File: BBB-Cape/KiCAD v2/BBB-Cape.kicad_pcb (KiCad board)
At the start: 2 copper layers, 54.6 x 86.4 mm, 85 parts, among them J1 MOUNTING_HOLE, J10 Conn_01x02, J11 RJ45-TRANSFO, J12 DB9_Female, J2 MOUNTING_HOLE, J3 MOUNTING_HOLE, J4 MOUNTING_HOLE, J5 MOUNTING_HOLE, J6 MOUNTING_HOLE, J7 MOUNTING_HOLE, J8 MOUNTING_HOLE, J9 01x06_Stackable Header, P1 02x23_Stackable Header, P2 02x23_Stackable Header, SW1 W5500_RST, SW2 SYS_RST, SW3 Power, U1 LM25576MH, U2 WIZnet W5500, U3 MAX13433EETD, Y1 25MHz

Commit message: Layout start for Rev3
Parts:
- moved P1 76.2 mm to (112.6, 67.2)
- moved P2 75.7 mm to (160.8, 67.2)
- moved J9 72.0 mm to (119.1, 90.1)
- moved J1 1.96 mm to (113.9, 62.1)
- moved J4 1.54 mm to (117.0, 128.2)
- moved J3 1.30 mm to (158.9, 128.2)
- moved J2 0.92 mm to (162.2, 62.1)
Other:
- outline, holes or cut-outs redrawn
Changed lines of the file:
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@@
     (area 110.592799 47.458559 165.352801 198.739687)
     (thickness 1.6)
-    (drawings 11)
+    (drawings 12)
     (tracks 0)
     (zones 0)
@@
   )
   (module Mounting_Holes:MountingHole_3.2mm_M3_Pad (layer F.Cu)
-    (at 115.2398 63.5381)
+    (at 113.8578 62.1461)
     (descr "Mounting Hole 3.2mm, M3")
     (tags "mounting hole 3.2mm m3")
@@
   )
   (module Mounting_Holes:MountingHole_3.2mm_M3_Pad (layer F.Cu)
-    (at 161.9758 63.0301)
+    (at 162.2378 62.1461)
     (descr "Mounting Hole 3.2mm, M3")
     (tags "mounting hole 3.2mm m3")
@@
   )
   (module Mounting_Holes:MountingHole_3.2mm_M3_Pad (layer F.Cu)
-    (at 157.7848 128.8161)
+    (at 158.9078 128.1561)
     (descr "Mounting Hole 3.2mm, M3")
     (tags "mounting hole 3.2mm m3")
@@
   )
   (module Mounting_Holes:MountingHole_3.2mm_M3_Pad (layer F.Cu)
-    (at 118.4148 127.5461)
+    (at 117.0078 128.1761)
     (descr "Mounting Hole 3.2mm, M3")
     (tags "mounting hole 3.2mm m3")
@@
   )
   (module Pin_Headers:Pin_Header_Straight_1x06_Pitch2.54mm (layer F.Cu)
-    (at 137.9728 159.619499)
+    (at 119.1078 90.0961)
     (descr "Through hole straight pin header, 1x06, 2.54mm pitch, single row")
     (tags "Through hole pin header THT 1x06 2.54mm single row")
@@
   )
   (module Pin_Headers:Pin_Header_Straight_2x23_Pitch2.54mm (layer F.Cu)
-    (at 137.9728 139.05789)
+    (at 112.5678 67.2161)
     (descr "Through hole straight pin header, 2x23, 2.54mm pitch, double rows")
     (tags "Through hole pin header THT 2x23 2.54mm double row")
@@
   )
   (module Pin_Headers:Pin_Header_Straight_2x23_Pitch2.54mm (layer F.Cu)
-    (at 137.9728 139.400687)
+    (at 160.8278 67.2161)
     (descr "Through hole straight pin header, 2x23, 2.54mm pitch, double rows")
     (tags "Through hole pin header THT 2x23 2.54mm double row")
@@
     )
   )
+  (gr_line (start 122.8178 133.8961) (end 153.5678 133.8961) (layer Edge.Cuts) (width 0.15))
+  (gr_line (start 110.6678 53.8961) (end 110.6678 121.2061) (layer Edge.Cuts) (width 0.15))
+  (gr_line (start 132.1278 47.5361) (end 117.1078 47.5361) (layer Edge.Cuts) (width 0.15))
+  (gr_line (start 148.3878 47.5361) (end 159.0078 47.5361) (layer Edge.Cuts) (width 0.15))
+  (gr_line (start 165.2778 121.2061) (end 165.2778 53.8861) (layer Edge.Cuts) (width 0.15))
   (gr_line (start 148.3878 67.2161) (end 148.3878 47.5361) (layer Edge.Cuts) (width 0.15))
   (gr_line (start 132.1278 67.2161) (end 148.3838 67.2161) (layer Edge.Cuts) (width 0.15))
@@
   (gr_arc (start 123.3678 121.20626) (end 110.6678 121.20626) (angle -87.47303961) (layer Edge.Cuts) (width 0.15))
   (gr_arc (start 152.56764 121.22404) (end 165.2778 121.2215) (angle 85.5529637) (layer Edge.Cuts) (width 0.15))
-  (gr_line (start 165.2778 133.89356) (end 165.2778 47.53356) (layer Edge.Cuts) (width 0.15))
-  (gr_line (start 110.6678 133.89356) (end 165.2778 133.89356) (layer Edge.Cuts) (width 0.15))
-  (gr_line (start 110.6678 47.53356) (end 165.2778 47.53356) (layer Edge.Cuts) (width 0.15))
-  (gr_line (start 110.6678 133.89356) (end 110.6678 47.53356) (layer Edge.Cuts) (width 0.15))
 )

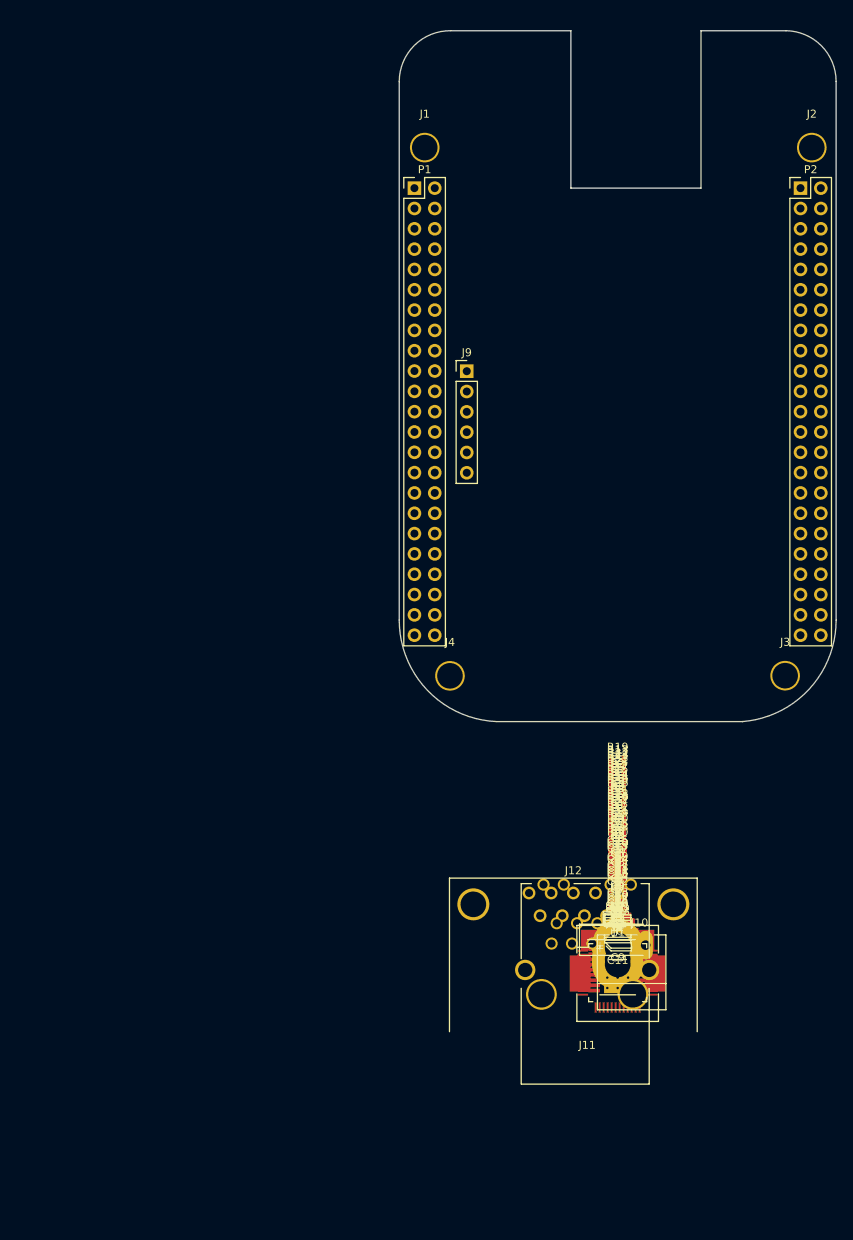
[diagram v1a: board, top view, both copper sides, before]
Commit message: Layout Update
Changed RJ45 connector to a surface mount component. Need to properly reposition P8 and P9.
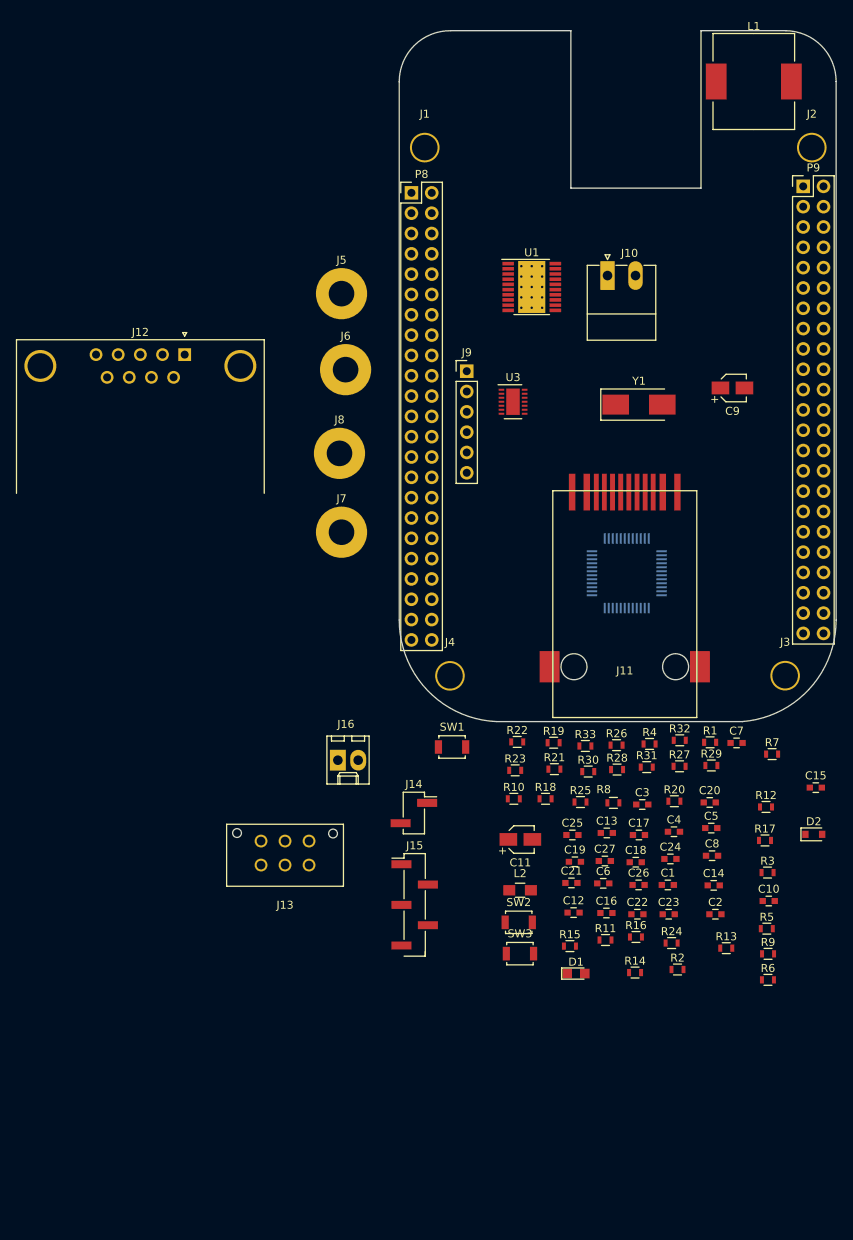
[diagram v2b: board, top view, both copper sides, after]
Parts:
- removed P1, P2: 02x23_Stackable Header, Pin_Headers:Pin_Header_Straight_2x23_Pitch2.54mm
- added J13: SPI1, Connectors_Molex:Molex_Microfit3_Header_02x03_Straight_43045-0628, F.Cu at (99.4, 151.8)
- added J14: I2C2, Pin_Headers:Pin_Header_Straight_1x02_Pitch2.54mm_SMD_Pin1Right, F.Cu at (112.5, 145.3)
- added J15: UART5, Pin_Headers:Pin_Header_Straight_1x05_Pitch2.54mm_SMD_Pin1Left, F.Cu at (112.6, 156.8)
- added J16: 5V PWR, Connectors_Molex:Molex_KK-6410-02_02x2.54mm_Straight, F.Cu at (103.0, 138.7)
- added P8: 02x23_Stackable Header, Pin_Headers:Pin_Header_Straight_2x23_Pitch2.54mm, F.Cu at (112.2, 67.8)
- added P9: 02x23_Stackable Header, Pin_Headers:Pin_Header_Straight_2x23_Pitch2.54mm, F.Cu at (161.2, 67.0)
- J11: footprint Connectors:RJ45_TRANSFO -> RJ45:RJ45_Surface_Mount
- U2: moved to B.Cu
- moved L1 112.8 mm to (155.0, 53.9)
- moved J5 88.5 mm to (103.5, 80.4)
- moved J12 86.4 mm to (83.8, 88.0)
- moved U1 85.7 mm to (127.2, 79.6)
- moved J10 83.7 mm to (136.7, 78.1)
- moved J6 81.8 mm to (104.0, 89.9)
- moved J8 72.1 mm to (103.2, 100.4)
- moved C9 69.8 mm to (152.3, 92.2)
- moved U3 68.9 mm to (124.9, 93.9)
- moved Y1 67.0 mm to (140.6, 94.3)
- moved J7 62.4 mm to (103.5, 110.2)
- moved U2 49.9 mm to (139.1, 115.4)
- moved J11 32.1 mm to (138.9, 127.0)
- moved SW1 30.5 mm to (117.3, 137.1)
- moved C15 29.3 mm to (162.7, 142.2)
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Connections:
- J11 pad 8: (no net) -> Net-(J11-Pad8)
- J12 pad 6: (no net) -> Net-(J12-Pad6)
- J12 pad 7: (no net) -> Net-(J12-Pad7)
- J12 pad 8: (no net) -> Net-(J12-Pad8)
- J12 pad 9: (no net) -> Net-(J12-Pad9)
- J9 pad 1: DGND -> Net-(J9-Pad1)
- J9 pad 2: (no net) -> Net-(J9-Pad2)
- J9 pad 3: (no net) -> Net-(J9-Pad3)
- J9 pad 4: (no net) -> UART0_RXD
- J9 pad 5: (no net) -> UART0_TXD
- J9 pad 6: (no net) -> Net-(J9-Pad6)
- U1 pad 2: (no net) -> Net-(U1-Pad2)
- U1 pad 5: (no net) -> Net-(U1-Pad5)
- U2 pad 12: (no net) -> Net-(U2-Pad12)
- U2 pad 13: (no net) -> Net-(U2-Pad13)
- U2 pad 18: (no net) -> Net-(U2-Pad18)
- U2 pad 24: (no net) -> Net-(U2-Pad24)
- U2 pad 26: (no net) -> Net-(U2-Pad26)
- U2 pad 32: SPI1_CS0 -> I2C1_SCL/SPI0_CS0
- U2 pad 33: SPI1_SCLK -> I2C2_SDA/SPIO_SCLK/UART2_RXD
- U2 pad 34: SPI1_DI -> I2C1_SDA/SPI0_DI
- U2 pad 35: SPI1_D0 -> I2C2_SCL/SPI0_DO/UART2_TXD
- U2 pad 46: (no net) -> Net-(U2-Pad46)
- U2 pad 47: (no net) -> Net-(U2-Pad47)
- U2 pad 7: (no net) -> Net-(U2-Pad7)
- U3 pad 13: (no net) -> Net-(U3-Pad13)
- U3 pad 7: (no net) -> Net-(U3-Pad7)

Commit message: Layout Fix
Updated a few footprints, fixed the positioning of P8 and P9, and adjusted general layout a bit.
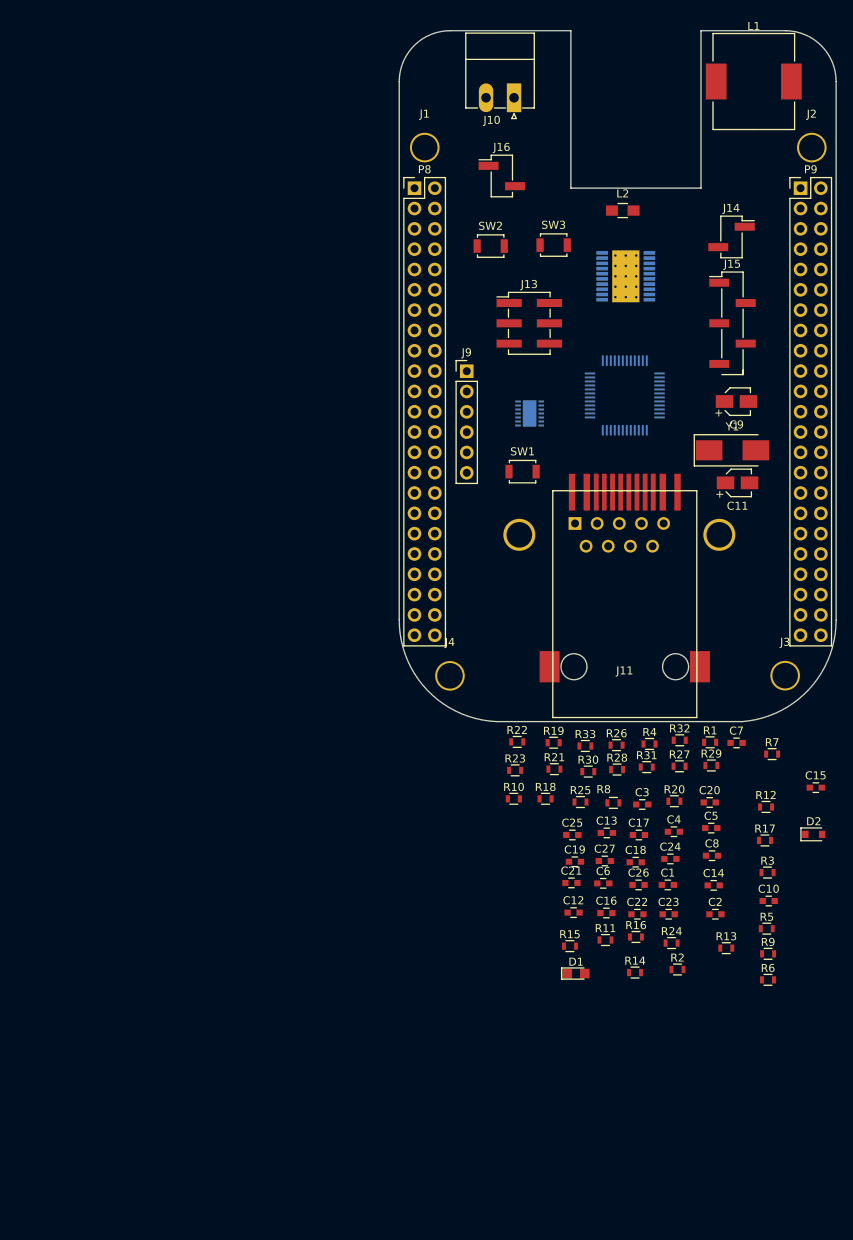
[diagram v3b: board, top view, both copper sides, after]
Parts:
- removed J5, J6, J7, J8: MOUNTING_HOLE, Mounting_Holes:MountingHole_3.2mm_M3_Pad
- J12, U1, U3: moved to B.Cu
- J13: footprint Connectors_Molex:Molex_Microfit3_Header_02x03_Straight_43045-0628 -> Pin_Headers:Pin_Header_Straight_2x03_Pitch2.54mm_SMD
- J16: footprint Connectors_Molex:Molex_KK-6410-02_02x2.54mm_Straight -> Pin_Headers:Pin_Header_Straight_1x02_Pitch2.54mm_SMD_Pin1Left
- moved SW3 88.7 mm to (130.0, 74.3)
- moved L2 85.9 mm to (138.6, 70.0)
- moved SW2 84.6 mm to (122.1, 74.5)
- moved J15 82.8 mm to (152.3, 84.1)
- moved J14 82.2 mm to (152.2, 73.3)
- moved J16 75.8 mm to (123.5, 65.7)
- moved J13 73.1 mm to (126.9, 84.1)
- moved J12 53.2 mm to (132.6, 109.1), turned to 180 degrees
- moved C11 52.2 mm to (153.0, 104.1)
- moved SW1 35.5 mm to (126.1, 102.7)
- moved J10 25.1 mm to (125.0, 55.9), turned to 180 degrees
- moved U2 22.2 mm to (138.9, 93.1)
- moved Y1 13.0 mm to (152.3, 100.0)
- moved U1 11.8 mm to (139.0, 78.2), turned to 180 degrees
- moved U3 2.54 mm to (127.0, 95.4)
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
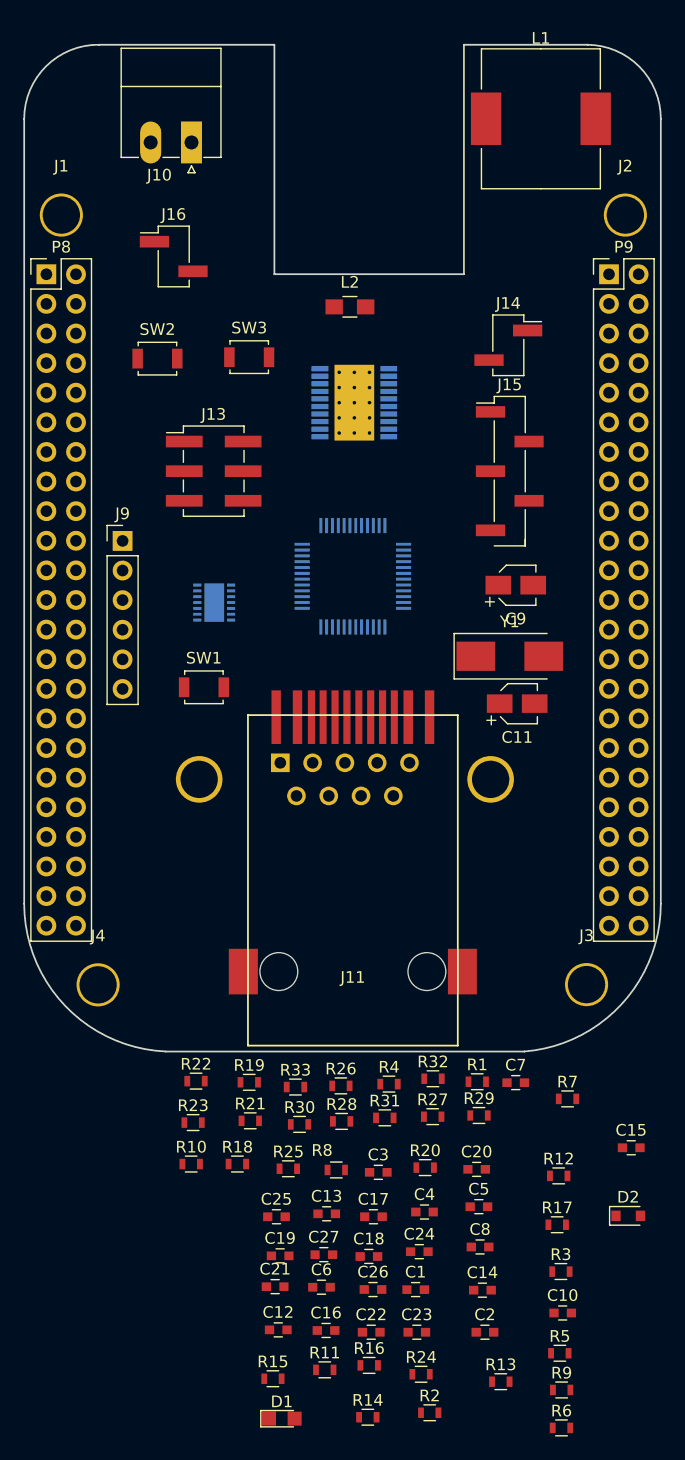
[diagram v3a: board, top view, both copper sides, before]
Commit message: Layout Update
Initial resistor placement. Fixed ethernet connector and RS485 connector position.
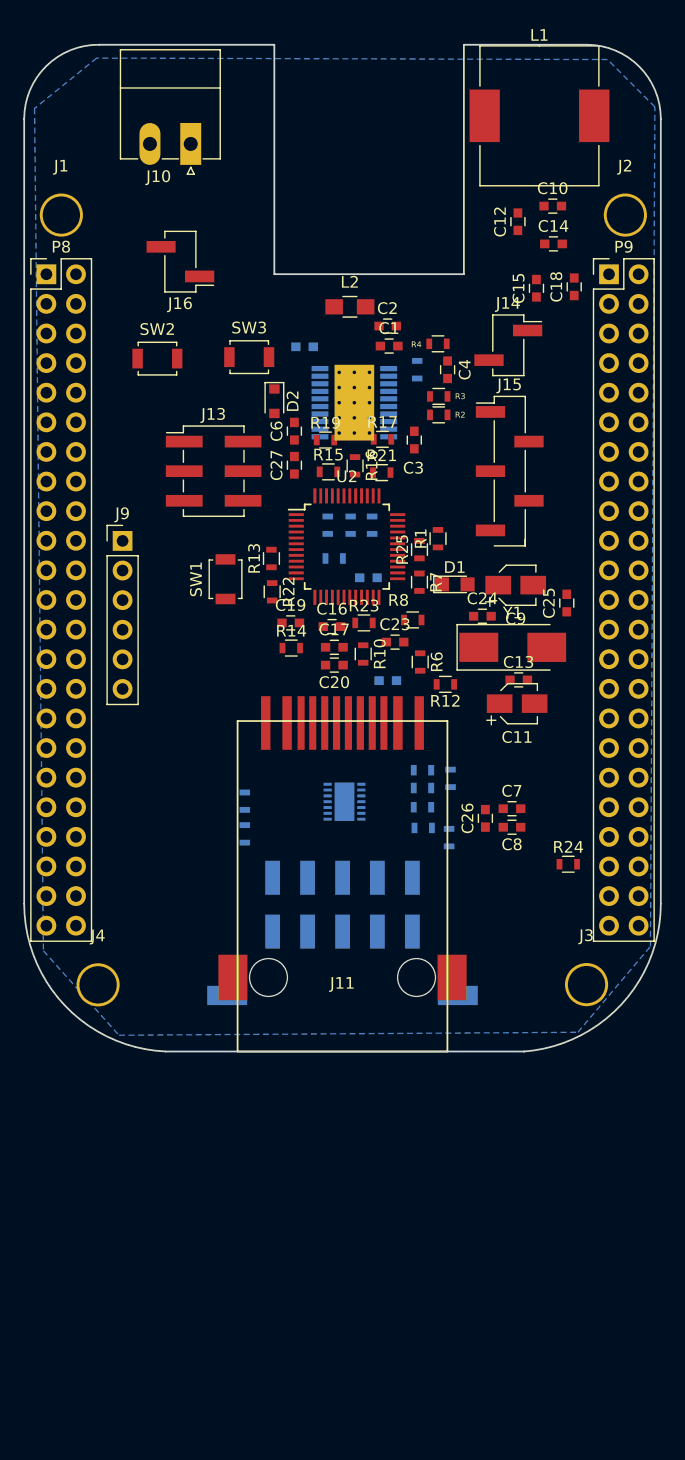
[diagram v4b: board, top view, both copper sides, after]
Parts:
- C21, C22, C5, R11, R18, R20, R26, R27, R28, R29, R30, R31, R32, R33, R5, R9: moved to B.Cu
- J12: footprint Connectors_DSub:DSUB-9_Female_Horizontal_Pitch2.77x2.84mm_EdgePinOffset14.56mm_Housed_MountingHolesOffset15.98mm -> Connectors_Molex:Molex_MicroFit_3.0-43045-1010_10x3.00mm_Angled
- U2: moved to F.Cu
- moved C12 97.3 mm to (153.0, 62.7), turned to 90 degrees
- moved C10 94.9 mm to (156.0, 61.4)
- moved C14 90.0 mm to (156.1, 64.6)
- moved C2 86.7 mm to (141.8, 71.7)
- moved R2 85.6 mm to (146.2, 79.3), turned to 180 degrees
- moved R5 85.2 mm to (144.4, 75.4), turned to 90 degrees
- moved C18 85.0 mm to (157.8, 68.3), turned to 90 degrees
- moved C1 81.0 mm to (142.0, 73.4)
- moved R15 77.9 mm to (136.8, 84.2)
- moved R16 77.2 mm to (139.1, 83.7), turned to 270 degrees
- moved R9 76.8 mm to (136.7, 88.7), turned to 90 degrees
- moved D2 76.2 mm to (132.1, 78.1), turned to 270 degrees
- moved R3 75.8 mm to (146.2, 77.7)
- moved C5 75.3 mm to (134.7, 73.4)
- moved C15 74.2 mm to (154.6, 68.4), turned to 90 degrees
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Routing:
- added copper zone on B.Cu, net DGND
